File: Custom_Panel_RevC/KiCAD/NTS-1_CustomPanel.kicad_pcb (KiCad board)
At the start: 2 copper layers, 128.5 x 78 mm, 67 parts, among them CN1 19x2 2.54mm header, CN10 1x4 2.54mm header, CN11 1x3 2.54mm header, CN2 1x7 2.54mm header, CN3 1x8 2.54mm connector, CN4 1x6 2.54mm connector, CN5 1x10 2.54mm connector, CN6 1x8 2.54mm connector, CN7 1x7 2.54mm header, CN8 19x2 2.54mm header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

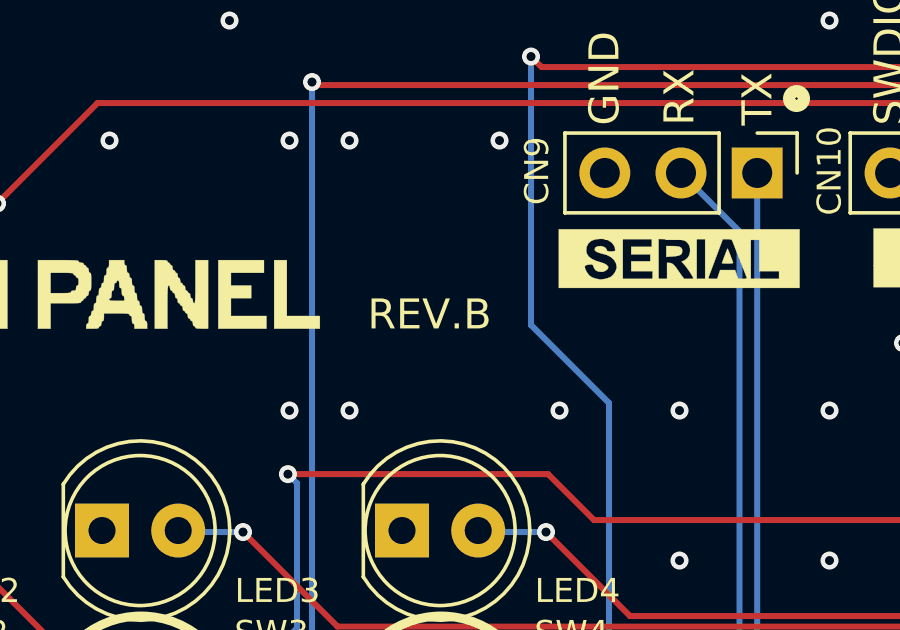
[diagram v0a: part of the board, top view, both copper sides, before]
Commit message: Rev.B data was actually Rev.C, fix some conflicting info in KiCAD files.
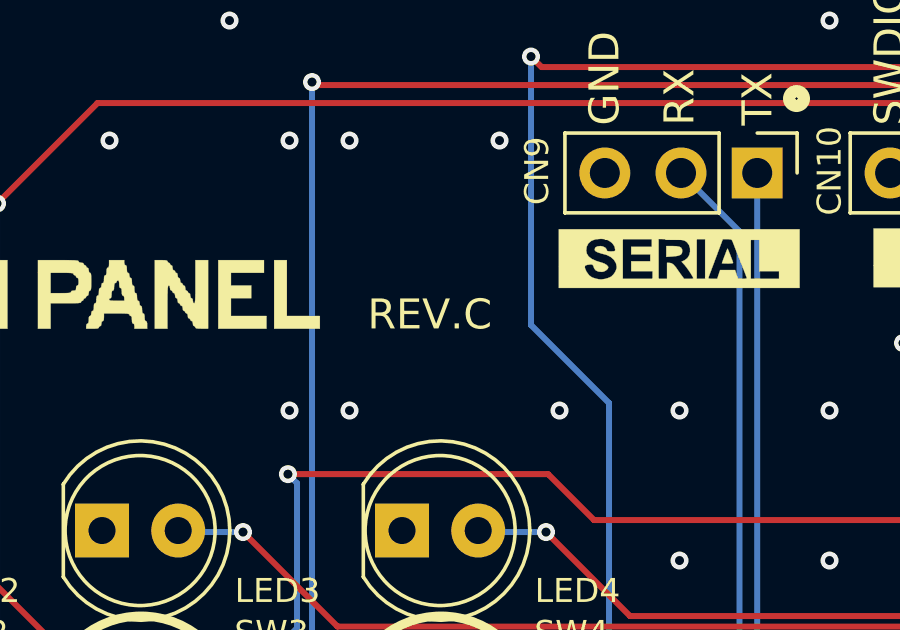
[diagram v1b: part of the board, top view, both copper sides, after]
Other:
- board text added: "REV.C"
- board text removed: "REV.B"
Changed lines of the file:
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@@
     (title "NTS-1 Custom Panel PCB")
     (date 2019-12-27)
-    (rev A)
+    (rev C)
+    (company "KORG INC.")
     (comment 1 "NTS-1 digital kit")
     (comment 2 "Kazuya Miura")
@@
   )
   (setup
-    (last_trace_width 0.3)
+    (last_trace_width 0.2)
     (user_trace_width 0.2)
     (user_trace_width 0.3)
@@
     (effects (font (size 0.1 0.1) (thickness 0.1)) (justify left))
   )
-  (gr_text REV.B (at 144.59948 83.79999) (layer F.SilkS)
+  (gr_text REV.C (at 144.59948 83.79999) (layer F.SilkS)
     (effects (font (size 1 1) (thickness 0.1)) (justify left))
   )

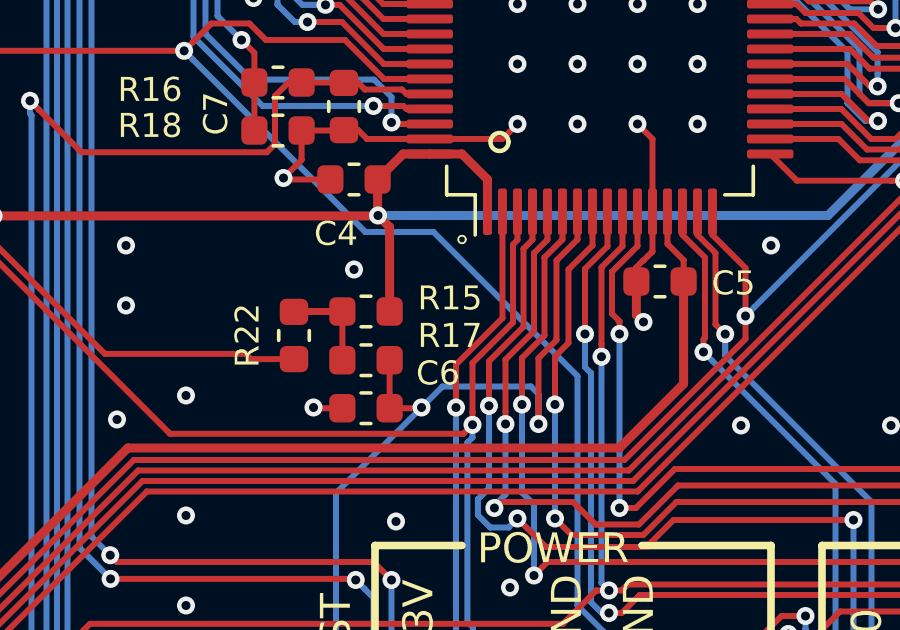
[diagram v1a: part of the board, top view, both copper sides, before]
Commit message: [revC] Lower power stabilizing capacitor to 1u.
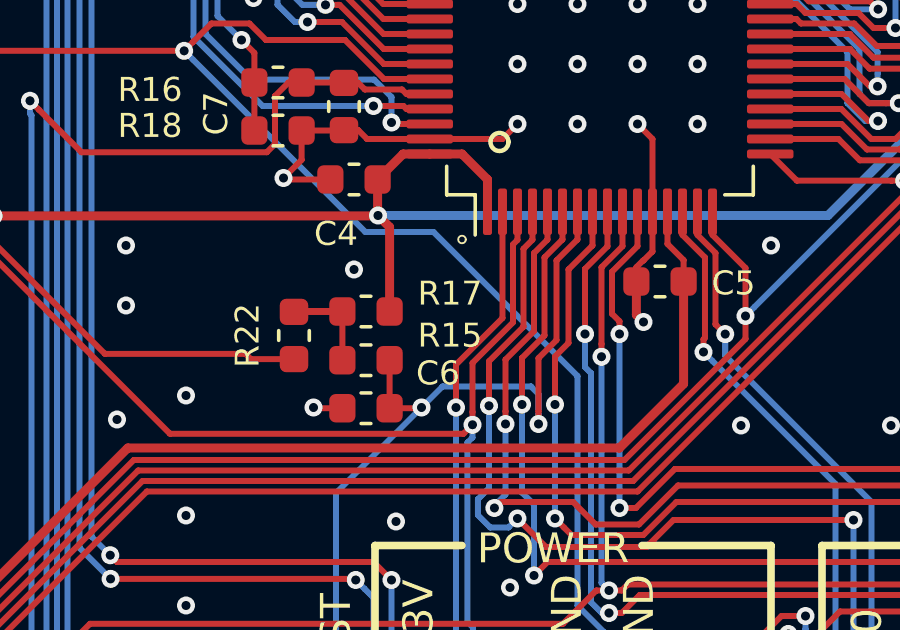
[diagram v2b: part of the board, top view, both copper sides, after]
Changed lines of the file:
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@@
     (tags resistor)
     (attr smd)
-    (fp_text reference R15 (at 2.80052 -2.06499 unlocked) (layer F.SilkS)
+    (fp_text reference R15 (at 2.80052 -0.82499 unlocked) (layer F.SilkS)
       (effects (font (size 0.8 0.8) (thickness 0.15)))
     )
@@
     (tags resistor)
     (attr smd)
-    (fp_text reference R17 (at -2.80052 -0.81009 unlocked) (layer F.SilkS)
+    (fp_text reference R17 (at -2.80052 0.59991 unlocked) (layer F.SilkS)
       (effects (font (size 0.8 0.8) (thickness 0.15)))
     )
